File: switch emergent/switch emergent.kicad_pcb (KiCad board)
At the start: 2 copper layers, 38.5 x 58.4 mm, 35 parts, among them J1 Conn_02x04_Odd_Even, J2 Conn_01x06, J3 Conn_01x09, J4 Conn_01x10, J5 Conn_01x10

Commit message: v0.2 Ordered
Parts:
- removed D3: LED, LED_SMD:LED_0603_1608Metric_Pad1.05x0.95mm_HandSolder
- removed R7: 240, Resistor_SMD:R_0603_1608Metric_Pad0.98x0.95mm_HandSolder
- moved D6 5.16 mm to (64.8, 103.3), turned to 90 degrees
- moved R1 4.06 mm to (88.4, 102.5), turned to -90 degrees
- moved R11 3.85 mm to (67.3, 104.2), turned to 0 degrees
- moved R2 2.59 mm to (67.3, 102.6), turned to 0 degrees
- moved D5 2.35 mm to (90.2, 102.4), turned to 90 degrees
- moved R10 0.55 mm to (89.3, 105.0), turned to 180 degrees
- moved C2 0.10 mm to (72.2, 101.2)
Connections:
- D5 pad 2: VBUS -> +3.3V
- D6 pad 2: VBUS -> +3.3V
- J3 pad 3: Net-(J3-Pin_3) -> +3.3V
- R1 pad 1: VBUS -> +3.3V
- R2 pad 1: VBUS -> +3.3V
- U3 pad 30: Net-(J3-Pin_3) -> +3.3V
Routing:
- net +3.3V: track 0.00 -> 73.1 mm, vias 0 -> 2
- net Net-(J3-Pin_3): track 10.3 -> 0.00 mm
- net VBUS: track 70.0 -> 61.5 mm, vias 4 -> 1
- net EN2: track 12.9 -> 16.6 mm, vias 0 -> 1
- net nFLT2: track 22.0 -> 18.4 mm, vias 0 -> 1
- net GND: track 23.1 -> 25.3 mm, vias 97 -> 108
- net Net-(D3-K): track 1.67 -> 0.00 mm

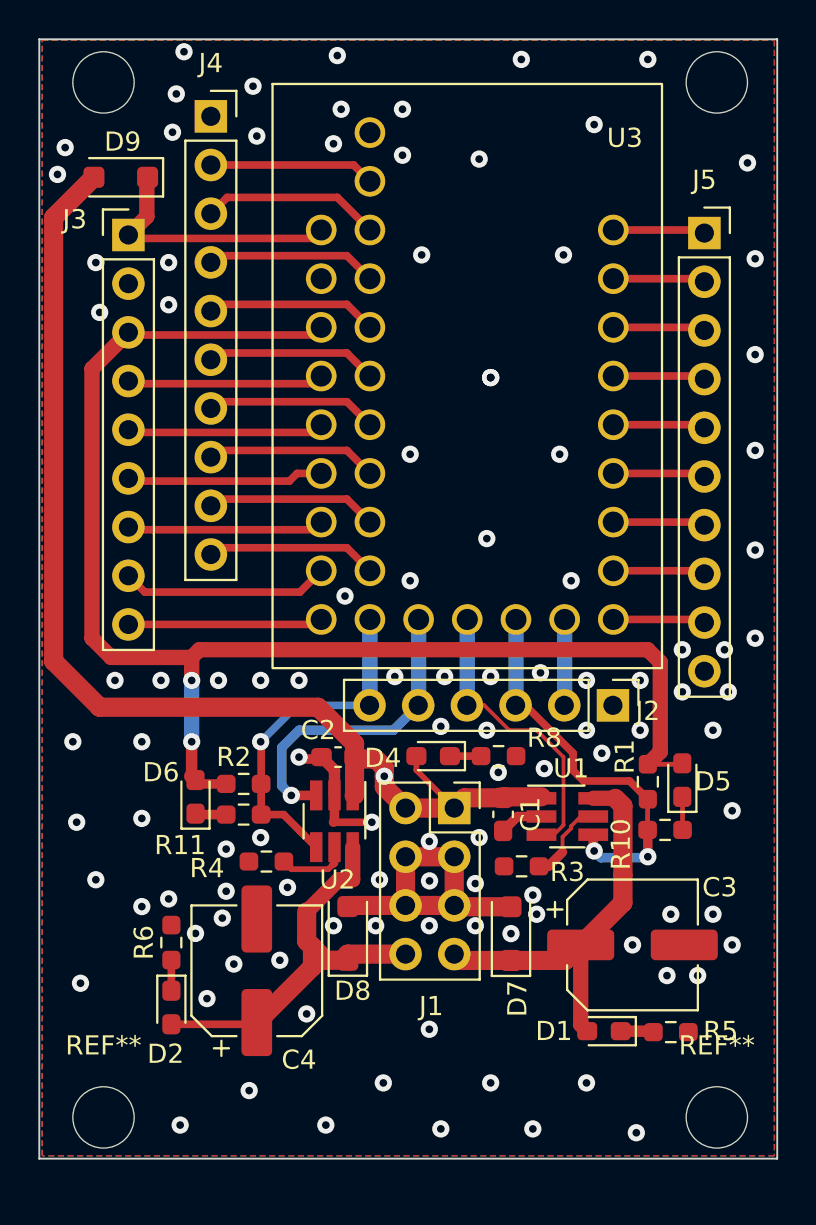
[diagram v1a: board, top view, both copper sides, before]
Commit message: v0.3 universal PCB for embedded and remote swithces
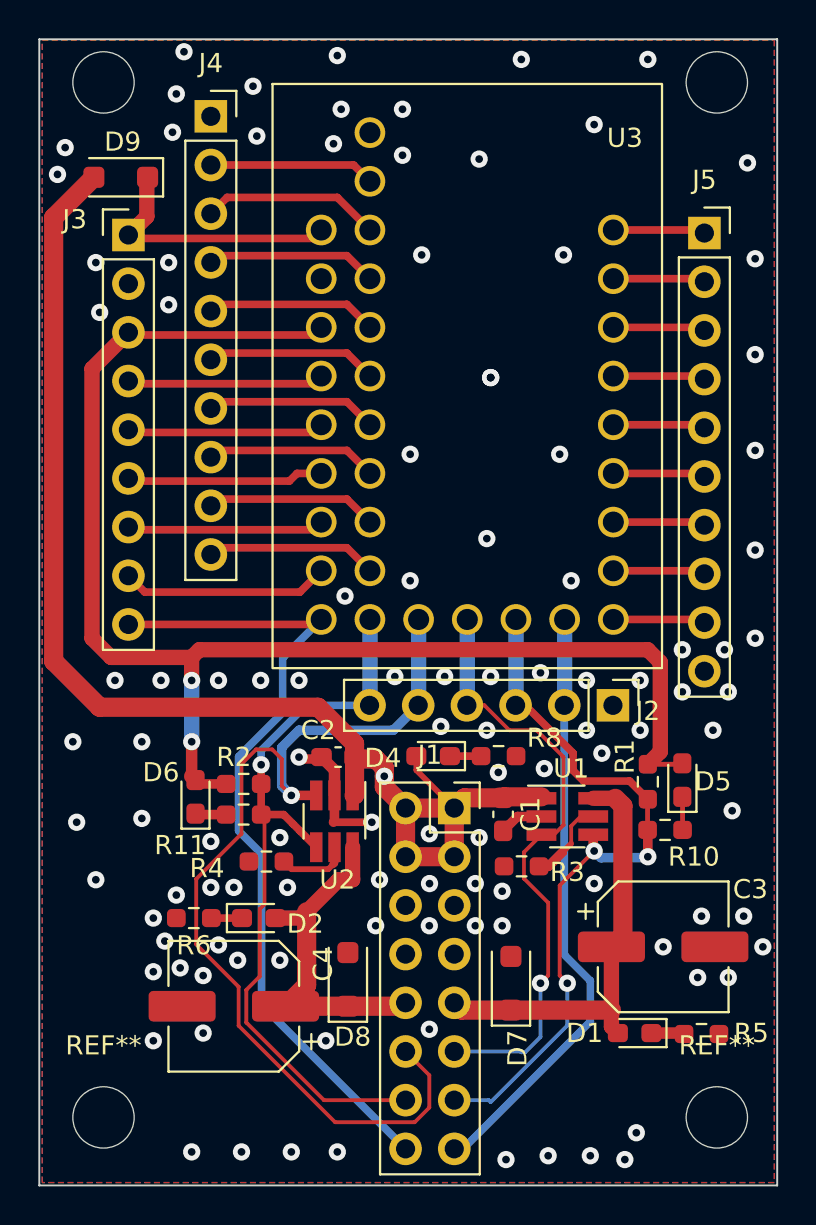
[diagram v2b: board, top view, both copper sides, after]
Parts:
- J1: value Conn_02x04_Odd_Even -> Conn_02x08_Odd_Even; footprint Connector_PinSocket_2.54mm:PinSocket_2x04_P2.54mm_Vertical -> Connector_PinSocket_2.54mm:PinSocket_2x08_P2.54mm_Vertical
- moved D2 6.52 mm to (68.1, 109.6), turned to 0 degrees
- moved D7 2.59 mm to (81.3, 113.0)
- moved D8 2.40 mm to (72.8, 112.8)
- moved C4 2.21 mm to (66.8, 114.2), turned to 180 degrees
- moved R6 1.73 mm to (64.7, 109.6), turned to 180 degrees
- moved R5 1.60 mm to (91.2, 115.7)
- moved C3 1.60 mm to (89.2, 111.1)
- moved D1 1.60 mm to (87.7, 115.6)
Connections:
- J1 pad 3: GND -> VBUS
- J1 pad 4: GND -> VBUS
- J1 pad 7: VOUT1 -> GND
- J1 pad 8: VOUT2 -> GND
- J2 pad 2: Net-(J2-Pin_2) -> BTN1
- J3 pad 9: Net-(J3-Pin_9) -> BTN2
- U3 pad 14: Net-(J3-Pin_9) -> BTN2
- U3 pad 9: Net-(J2-Pin_2) -> BTN1
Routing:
- net BTN2: track 0.00 -> 43.2 mm
- net EN2: track 16.6 -> 52.6 mm
- net BTN1: track 0.00 -> 31.4 mm
- net nFLT2: track 18.4 -> 40.3 mm
- net nFLT1: track 20.8 -> 38.4 mm, vias 2 -> 3
- net EN1: track 15.6 -> 32.0 mm, vias 0 -> 1
- net GND: track 25.3 -> 9.33 mm, vias 108 -> 111
- net Net-(J3-Pin_9): track 10.2 -> 0.00 mm
- net VBUS: track 61.5 -> 69.1 mm
- net Net-(J2-Pin_2): track 4.52 -> 0.00 mm
- net VOUT2: track 21.7 -> 18.3 mm
- net VOUT1: track 21.6 -> 22.3 mm
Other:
- board size 38.5 x 58.4 mm -> 38.5 x 59.8 mm

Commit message: v0.4 PCB uluchshaizing
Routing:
- net BTN2: track 43.2 -> 53.9 mm
- net BTN1: track 31.4 -> 32.1 mm
- net nFLT1: track 38.4 -> 39.0 mm
- net GND: vias 111 -> 127

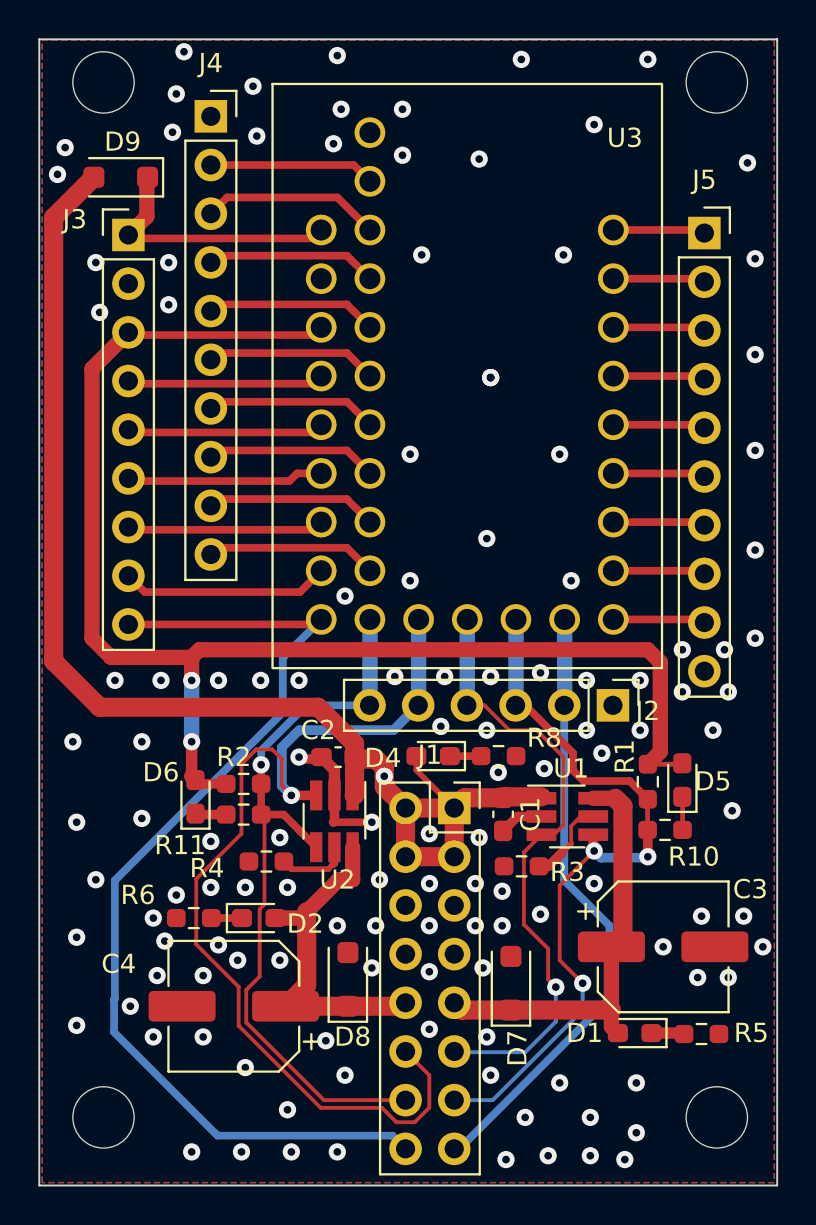
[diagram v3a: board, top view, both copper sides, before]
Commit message: v0.5 ordered advanced with embedded and remote switches
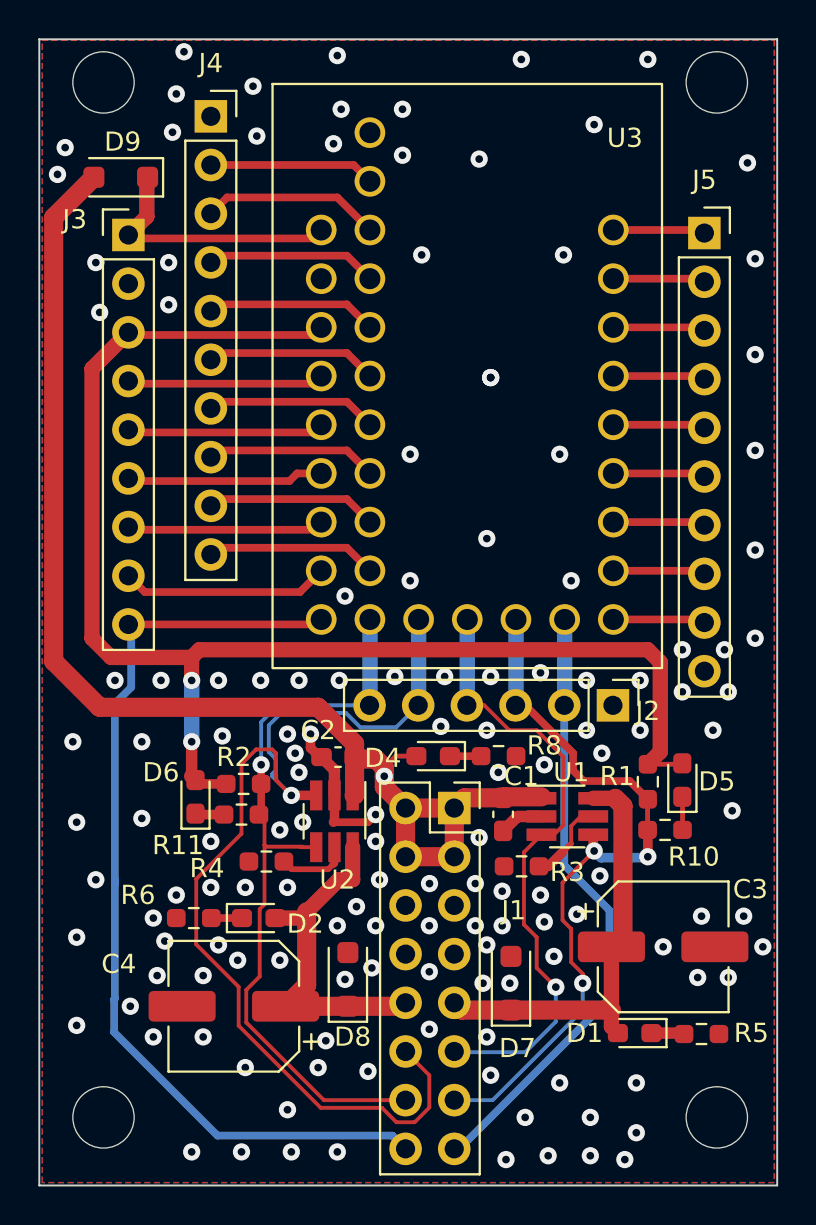
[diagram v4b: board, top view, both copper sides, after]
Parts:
- moved R11 0.11 mm to (67.2, 104.2)
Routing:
- net BTN2: track 53.9 -> 49.8 mm
- net EN2: track 52.6 -> 55.0 mm
- net VBUS: track 69.1 -> 67.5 mm
- net nFLT2: track 40.3 -> 39.5 mm
- net GND: track 9.33 -> 10.0 mm, vias 127 -> 141
